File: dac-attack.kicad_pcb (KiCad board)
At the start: 2 copper layers, 31.1 x 43.8 mm, 59 parts, among them J1 BOARD, J2 BOARD, J3 BOARD, J4 ANALOG, J5 DIGITAL, J6 USER, J7 BTN, U1 CS8416-xZZ, U2 PCM5100, U3 SD6210A, U4 XC6206P332MR, U5 XC6206P332MR

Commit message: Initial work on revision 2023b.
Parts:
- removed the J2 at (95.2, 104.1)
- removed the J6 at (92.7, 90.8)
- removed the R9 at (100.3, 108.6)
- added C25: 22nF, Capacitor_SMD:C_0402_1005Metric, F.Cu at (155.6, 79.6)
- added H1: MountingHole, MountingHole:MountingHole_3.2mm_M3, F.Cu at (107.3, 72.4)
- added H2: MountingHole, MountingHole:MountingHole_3.2mm_M3, F.Cu at (169.0, 72.4)
- added J5: USER, Connector_PinHeader_2.54mm:PinHeader_1x02_P2.54mm_Vertical, B.Cu at (148.6, 88.3)
- added J7: BTN, Connector_JST:JST_SH_SM02B-SRSS-TB_1x02-1MP_P1.00mm_Horizontal, F.Cu at (128.3, 87.5)
- added R10: 10K, Resistor_SMD:R_0402_1005Metric, F.Cu at (163.2, 85.7)
- added R8: 47K, Resistor_SMD:R_0402_1005Metric, F.Cu at (156.8, 68.6)
- added TP1: GND, TestPoint:TestPoint_Keystone_5000-5004_Miniature, F.Cu at (104.8, 67.3)
- added TP2: GND, TestPoint:TestPoint_Keystone_5000-5004_Miniature, F.Cu at (171.4, 67.3)
- added TP3: 5V, TestPoint:TestPoint_Pad_D1.0mm, F.Cu at (162.6, 66.7)
- added TP4: 3V3, TestPoint:TestPoint_Pad_D1.0mm, F.Cu at (137.8, 74.9)
- added TP5: 3V3A, TestPoint:TestPoint_Pad_D1.0mm, F.Cu at (116.8, 71.8)
- added U6: TCM809, Package_TO_SOT_SMD:SOT-23, F.Cu at (159.4, 69.8)
- J1: footprint Connector_PinSocket_2.54mm:PinSocket_2x02_P2.54mm_Vertical -> Connector_PinHeader_2.54mm:PinHeader_1x04_P2.54mm_Vertical; moved to B.Cu
- moved C15 90.6 mm to (160.0, 72.4)
- moved FB1 89.2 mm to (160.7, 77.5), turned to -90 degrees
- moved C1 86.7 mm to (158.8, 77.5), turned to 90 degrees
- moved C23 83.2 mm to (156.8, 75.6), turned to -90 degrees
- moved C16 82.6 mm to (155.6, 77.6), turned to 90 degrees
- moved C28 81.6 mm to (155.6, 75.6), turned to -90 degrees
- moved R9 81.5 mm to (156.2, 73.7), turned to 180 degrees
- moved R3 75.6 mm to (153.0, 69.8), turned to 180 degrees
- moved C6 74.8 mm to (169.7, 78.7), turned to 90 degrees
- moved U1 74.4 mm to (149.9, 76.2), turned to 180 degrees
- moved C10 73.8 mm to (171.6, 79.4), turned to 90 degrees
- moved J1 73.7 mm to (171.4, 88.3), turned to 90 degrees
- moved J2 72.5 mm to (156.8, 87.5)
- moved G*** 72.0 mm to (153.0, 72.4)
- moved U3 70.4 mm to (166.5, 79.4), turned to 0 degrees
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- renumbered C25 to C26, C26 to C27, C27 to C28, J3 to J2, J4 to J3, J5 to J4, J7 to J6, R8 to R9
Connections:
- net /DDAT renamed /D_OUT
- C15 pad 1: GND -> +3V3
- C15 pad 2: Net-(C15-Pad2) -> GND
- C24 pad 1: /DOUT -> /D_IN
- J1 pad 1: /BUTTON -> GND
- J1 pad 2: /DOUT -> /VIN
- J1 pad 3: GND -> /D_IN
- J1 pad 4: /VIN -> /BUTTON
- J2 pad 4: /DOUT -> /D_IN
- J2 pad MP: unconnected-(J3-PadMP) -> GND
- U1 pad 5: Net-(C15-Pad2) -> Net-(C25-Pad2)
- U1 pad 9: +3V3 -> Net-(R8-Pad2)
- U3 pad 1: /VIN -> +5V
- U3 pad 5: +5V -> /VIN
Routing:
- net +5V: track 22.9 -> 60.3 mm
- net /D_IN: track 0.00 -> 19.3 mm
- net /DOUT: track 18.6 -> 0.00 mm, vias 2 -> 0
- net +3.3VA: track 52.1 -> 33.6 mm
- net /BUTTON: track 37.2 -> 50.8 mm, vias 3 -> 4
- net +3V3: track 87.0 -> 73.7 mm
- net Net-(R8-Pad2): track 0.00 -> 11.7 mm, vias 0 -> 2
- net /USER: track 15.5 -> 4.57 mm, vias 2 -> 1
- net Net-(J7-Pad2): track 2.54 -> 12.8 mm, vias 0 -> 2
- net /VIN: track 35.9 -> 42.4 mm
- net Net-(R15-Pad1): track 7.03 -> 13.0 mm
- net Net-(R1-Pad1): track 9.21 -> 14.7 mm
- net /RIGHT: track 15.5 -> 11.3 mm
- net /ADAT: track 10.3 -> 13.9 mm
- net Net-(C24-Pad2): track 11.7 -> 8.20 mm
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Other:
- board size 31.1 x 43.8 mm -> 71.8 x 26 mm
- board text added: "3V"
- board text added: "B_READ"
- board text added: "D_IN"
- board text added: "EXT BUTTON"
- board text added: "GND"
- board text added: "Rev 2023b Licensed under CERN-OHL-S v2"
- board text removed: "BTN"
- board text removed: "Rev 2023a Licensed under CERN-OHL-S v2"
- board text removed: "←MEMORY ←CARD"

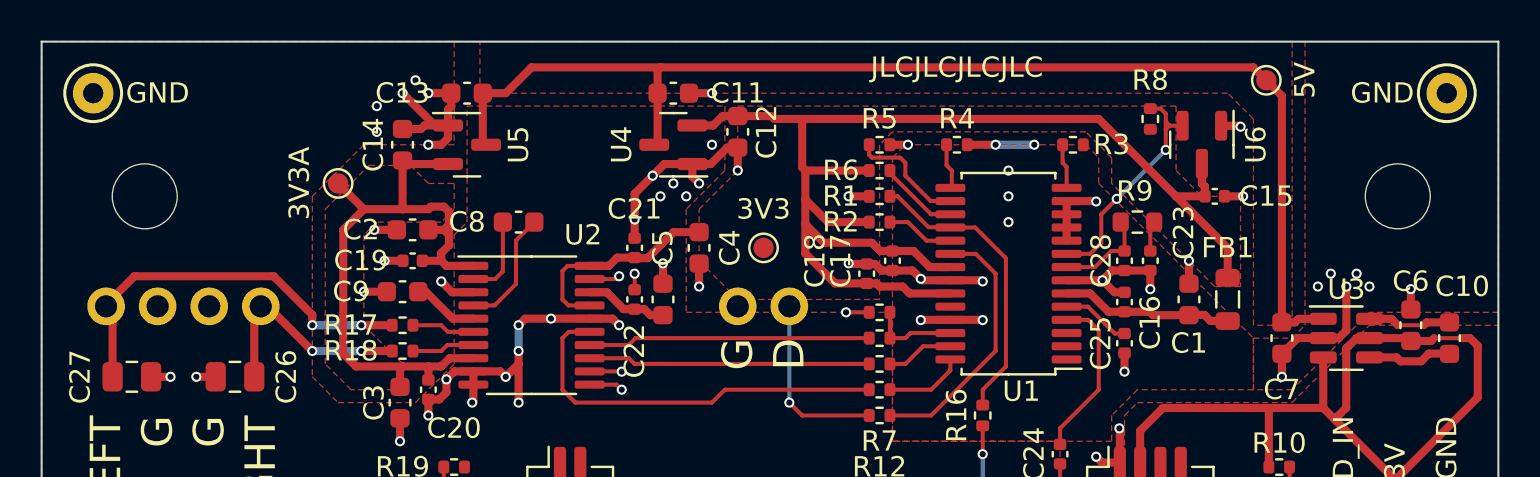
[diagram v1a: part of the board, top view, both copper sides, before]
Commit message: Tweaks to 2023b
Fixed one net, widened traces, made some minor silkscreen changes.
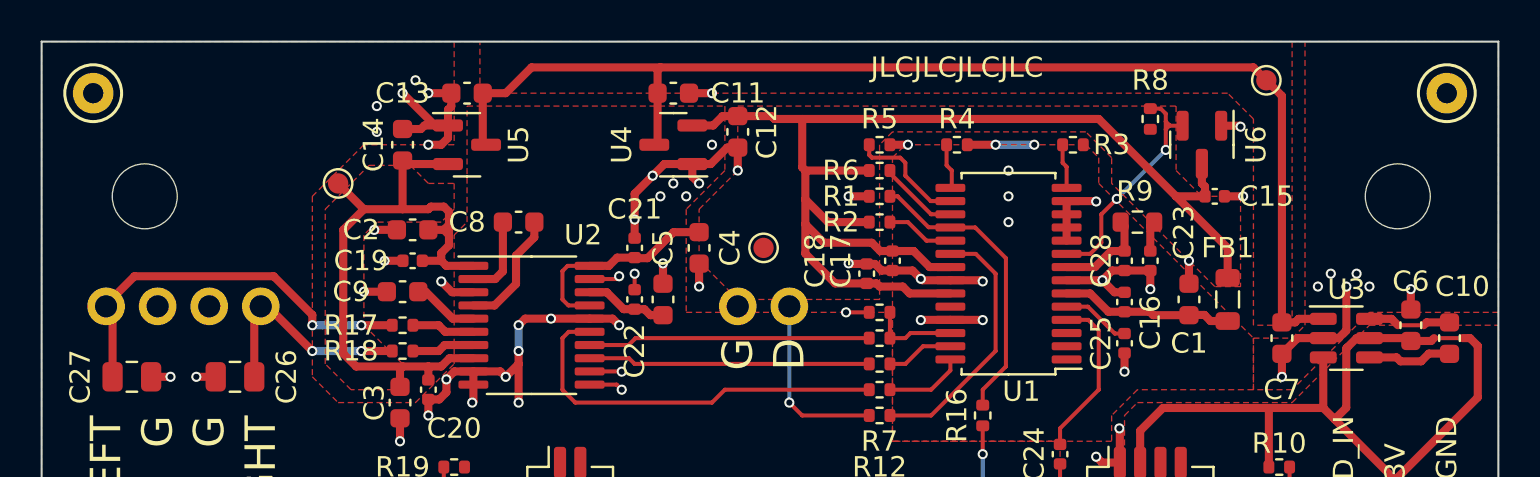
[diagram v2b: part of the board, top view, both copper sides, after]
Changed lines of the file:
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@@
   (net 39 "unconnected-(U1-Pad24)")
   (net 40 "Net-(R8-Pad2)")
-  (net 41 "Net-(J7-Pad2)")
+  (net 41 "Net-(J6-Pad2)")
   (net 42 "/D_IN")
   (net 43 "/D_OUT")
@@
       (net 18 "/BUTTON") (pinfunction "Pin_1") (pintype "passive"))
     (pad "2" smd roundrect (at 0.5 -2) (size 0.6 1.55) (layers "F.Cu" "F.Paste" "F.Mask") (roundrect_rratio 0.25)
-      (net 41 "Net-(J7-Pad2)") (pinfunction "Pin_2") (pintype "passive"))
+      (net 41 "Net-(J6-Pad2)") (pinfunction "Pin_2") (pintype "passive"))
     (pad "MP" smd roundrect (at 1.8 1.875) (size 1.2 1.8) (layers "F.Cu" "F.Paste" "F.Mask") (roundrect_rratio 0.2083333333)
       (net 2 "GND") (pinfunction "MountPin") (pintype "passive"))
@@
       (effects (font (size 1 1) (thickness 0.15)))
     )
-    (fp_text value "3V3" (at 0 1.905) (layer "F.SilkS")
+    (fp_text value "3V3" (at 0 1.905) (layer "F.SilkS") hide
       (effects (font (size 1 1) (thickness 0.15)))
     )
@@
       (effects (font (size 1 1) (thickness 0.15)))
     )
-    (fp_text value "GND" (at -3.175 0) (layer "F.SilkS")
+    (fp_text value "GND" (at -3.175 0) (layer "F.Fab")
       (effects (font (size 1 1) (thickness 0.15)))
     )
@@
       (effects (font (size 1 1) (thickness 0.15)))
     )
-    (fp_text value "GND" (at 3.175 0 180) (layer "F.SilkS")
+    (fp_text value "GND" (at 3.175 0 180) (layer "F.Fab")
       (effects (font (size 1 1) (thickness 0.15)))
     )
@@
     (property "Sheetname" "")
     (attr exclude_from_pos_files)
-    (fp_text reference "TP3" (at 0 -1.448) (layer "F.SilkS") hide
+    (fp_text reference "TP3" (at 0 -1.448) (layer "F.Fab") hide
       (effects (font (size 1 1) (thickness 0.15)))
     )
-    (fp_text value "5V" (at 1.905 0 90) (layer "F.SilkS")
+    (fp_text value "5V" (at 1.905 0 90) (layer "F.Fab")
       (effects (font (size 1 1) (thickness 0.15)))
     )
@@
       (net 2 "GND") (pintype "passive"))
     (pad "2" smd roundrect (at 0.51 0 180) (size 0.54 0.64) (layers "F.Cu" "F.Paste" "F.Mask") (roundrect_rratio 0.25)
-      (net 41 "Net-(J7-Pad2)") (pintype "passive"))
+      (net 41 "Net-(J6-Pad2)") (pintype "passive"))
     (model "${KICAD6_3DMODEL_DIR}/Resistor_SMD.3dshapes/R_0402_1005Metric.wrl"
       (offset (xyz 0 0 0))
@@
       (effects (font (size 1 1) (thickness 0.15)))
     )
-    (fp_text value "3V3A" (at -1.905 0 90) (layer "F.SilkS")
+    (fp_text value "3V3A" (at -1.905 0 90) (layer "F.Fab")
       (effects (font (size 1 1) (thickness 0.15)))
     )
@@
       (net 18 "/BUTTON") (pinfunction "Pin_1") (pintype "passive"))
     (pad "2" thru_hole oval (at 0 -2.54 90) (size 1.7 1.7) (drill 1) (layers *.Cu *.Mask)
-      (net 41 "Net-(J7-Pad2)") (pinfunction "Pin_2") (pintype "passive"))
+      (net 41 "Net-(J6-Pad2)") (pinfunction "Pin_2") (pintype "passive"))
     (model "${KICAD6_3DMODEL_DIR}/Connector_PinHeader_2.54mm.3dshapes/PinHeader_1x02_P2.54mm_Vertical.wrl"
       (offset (xyz 0 0 0))
@@
   (segment (start 123.965 67.31) (end 123.965 69.6875) (width 0.4) (layer "F.Cu") (net 7))
   (segment (start 132.715 66.04) (end 161.925 66.04) (width 0.4) (layer "F.Cu") (net 7))
-  (segment (start 124.955 73.66) (end 124.955 76.086) (width 0.2) (layer "F.Cu") (net 8))
-  (segment (start 124.576 76.465) (end 123.5025 76.465) (width 0.2) (layer "F.Cu") (net 8))
-  (segment (start 124.955 76.086) (end 124.576 76.465) (width 0.2) (layer "F.Cu") (net 8))
-  (segment (start 125.603 76.708) (end 125.603 74.562) (width 0.2) (layer "F.Cu") (net 9))
-  (segment (start 125.603 76.708) (end 124.546 77.765) (width 0.2) (layer "F.Cu") (net 9))
-  (segment (start 125.603 74.562) (end 126.505 73.66) (width 0.2) (layer "F.Cu") (net 9))
-  (segment (start 124.546 77.765) (end 123.5025 77.765) (width 0.2) (layer "F.Cu") (net 9))
+  (segment (start 124.576 76.465) (end 124.955 76.086) (width 0.4) (layer "F.Cu") (net 8))
+  (segment (start 124.955 76.086) (end 124.955 73.66) (width 0.4) (layer "F.Cu") (net 8))
+  (segment (start 123.5025 76.465) (end 124.576 76.465) (width 0.4) (layer "F.Cu") (net 8))
+  (segment (start 125.603 75.311) (end 125.603 76.708) (width 0.4) (layer "F.Cu") (net 9))
+  (segment (start 125.603 76.708) (end 124.546 77.765) (width 0.4) (layer "F.Cu") (net 9))
+  (segment (start 126.505 73.66) (end 126.505 74.409) (width 0.4) (layer "F.Cu") (net 9))
+  (segment (start 126.505 74.409) (end 125.603 75.311) (width 0.4) (layer "F.Cu") (net 9))
+  (segment (start 124.546 77.765) (end 123.5025 77.765) (width 0.4) (layer "F.Cu") (net 9))
   (segment (start 122.484 78.415) (end 121.158 77.089) (width 0.4) (layer "F.Cu") (net 10))
   (segment (start 123.5025 78.415) (end 122.484 78.415) (width 0.4) (layer "F.Cu") (net 10))
@@
   (segment (start 153.771 77.825) (end 155.095 79.149) (width 0.2) (layer "F.Cu") (net 13))
   (segment (start 152.7225 77.825) (end 153.771 77.825) (width 0.2) (layer "F.Cu") (net 13))
-  (segment (start 156.845 75.085) (end 156.845 73.85) (width 0.2) (layer "F.Cu") (net 14))
-  (segment (start 156.845 73.85) (end 157.035 73.66) (width 0.2) (layer "F.Cu") (net 14))
+  (segment (start 156.845 73.85) (end 157.035 73.66) (width 0.4) (layer "F.Cu") (net 14))
+  (segment (start 156.845 75.085) (end 156.845 73.85) (width 0.4) (layer "F.Cu") (net 14))
   (segment (start 154.305 81.915) (end 152.4 83.82) (width 0.2) (layer "F.Cu") (net 15))
   (segment (start 154.305 78.994) (end 154.305 81.915) (width 0.2) (layer "F.Cu") (net 15))
@@
   (segment (start 149.225 80.01) (end 146.05 83.185) (width 0.2) (layer "F.Cu") (net 29))
   (segment (start 146.9975 75.225) (end 148.25 75.225) (width 0.2) (layer "F.Cu") (net 29))
-  (segment (start 122.215 79.715) (end 121.92 80.01) (width 0.2) (layer "F.Cu") (net 30))
-  (segment (start 123.5025 79.715) (end 122.215 79.715) (width 0.2) (layer "F.Cu") (net 30))
-  (segment (start 121.92 80.01) (end 120.525 80.01) (width 0.2) (layer "F.Cu") (net 30))
+  (segment (start 122.088 79.715) (end 121.793 80.01) (width 0.4) (layer "F.Cu") (net 30))
+  (segment (start 121.793 80.01) (end 120.525 80.01) (width 0.4) (layer "F.Cu") (net 30))
+  (segment (start 123.5025 79.715) (end 122.088 79.715) (width 0.4) (layer "F.Cu") (net 30))
   (segment (start 131.49 79.375) (end 131.15 79.715) (width 0.2) (layer "F.Cu") (net 31))
   (segment (start 143 79.375) (end 131.49 79.375) (width 0.2) (layer "F.Cu") (net 31))
@@
   (segment (start 135.89 81.915) (end 135.255 82.55) (width 0.2) (layer "F.Cu") (net 32))
   (segment (start 143 81.915) (end 135.89 81.915) (width 0.2) (layer "F.Cu") (net 32))
-  (segment (start 123.5025 79.065) (end 122.245 79.065) (width 0.2) (layer "F.Cu") (net 33))
-  (segment (start 121.92 78.74) (end 120.525 78.74) (width 0.2) (layer "F.Cu") (net 33))
-  (segment (start 122.245 79.065) (end 121.92 78.74) (width 0.2) (layer "F.Cu") (net 33))
+  (segment (start 123.5025 79.065) (end 122.118 79.065) (width 0.4) (layer "F.Cu") (net 33))
+  (segment (start 122.118 79.065) (end 121.793 78.74) (width 0.4) (layer "F.Cu") (net 33))
+  (segment (start 121.793 78.74) (end 120.525 78.74) (width 0.4) (layer "F.Cu") (net 33))
   (segment (start 129.2275 80.365) (end 131.165 80.365) (width 0.2) (layer "F.Cu") (net 34))
   (segment (start 131.445 80.645) (end 131.165 80.365) (width 0.2) (layer "F.Cu") (net 34))
   (segment (start 143 80.645) (end 131.445 80.645) (width 0.2) (layer "F.Cu") (net 34))
-  (segment (start 155.575 73.85) (end 155.385 73.66) (width 0.2) (layer "F.Cu") (net 35))
-  (segment (start 154.912 75.085) (end 155.575 75.085) (width 0.2) (layer "F.Cu") (net 35))
-  (segment (start 152.7225 75.875) (end 154.122 75.875) (width 0.2) (layer "F.Cu") (net 35))
-  (segment (start 154.122 75.875) (end 154.912 75.085) (width 0.2) (layer "F.Cu") (net 35))
-  (segment (start 155.575 75.085) (end 155.575 73.85) (width 0.2) (layer "F.Cu") (net 35))
+  (segment (start 154.122 75.875) (end 154.912 75.085) (width 0.4) (layer "F.Cu") (net 35))
+  (segment (start 152.7225 75.875) (end 154.122 75.875) (width 0.4) (layer "F.Cu") (net 35))
+  (segment (start 155.575 75.085) (end 155.575 73.85) (width 0.4) (layer "F.Cu") (net 35))
+  (segment (start 154.912 75.085) (end 155.575 75.085) (width 0.4) (layer "F.Cu") (net 35))
+  (segment (start 155.575 73.85) (end 155.385 73.66) (width 0.4) (layer "F.Cu") (net 35))
   (segment (start 156.845 68.07) (end 157.355 68.07) (width 0.2) (layer "F.Cu") (net 40))
   (segment (start 153.883 75.225) (end 154.432 74.676) (width 0.2) (layer "F.Cu") (net 40))

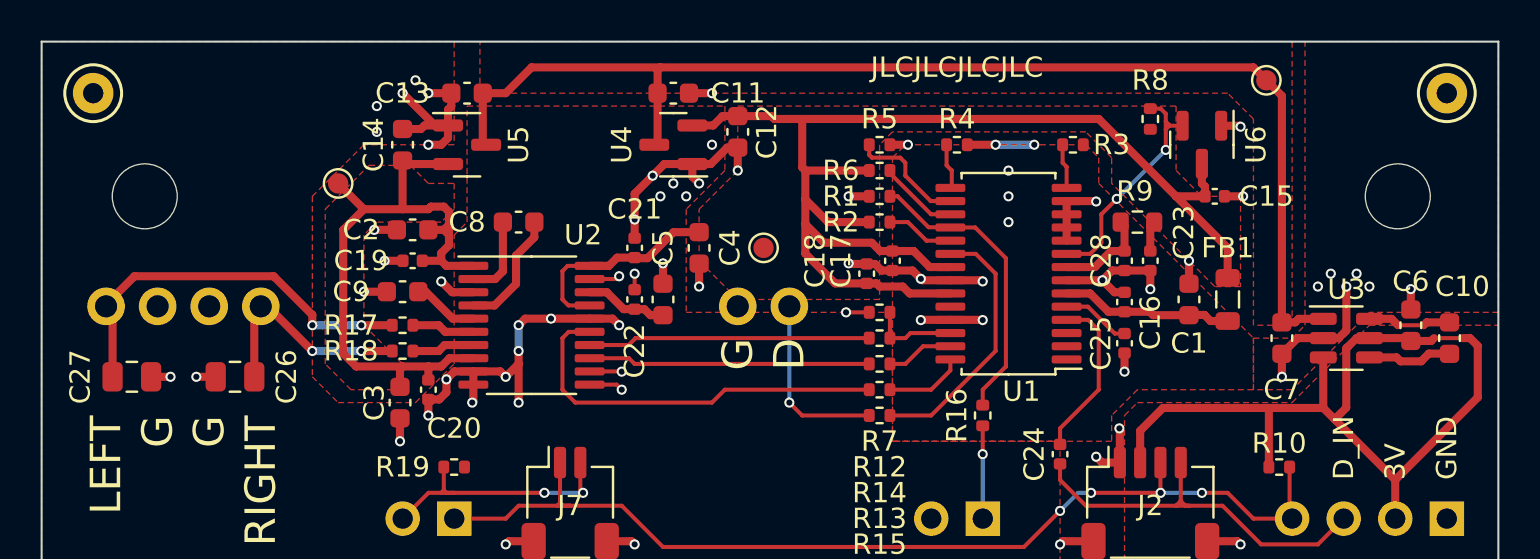
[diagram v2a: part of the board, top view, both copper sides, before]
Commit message: Board revision 2023c.
No component layout changes, just minor tweaks to mounting holes and silkscreening.
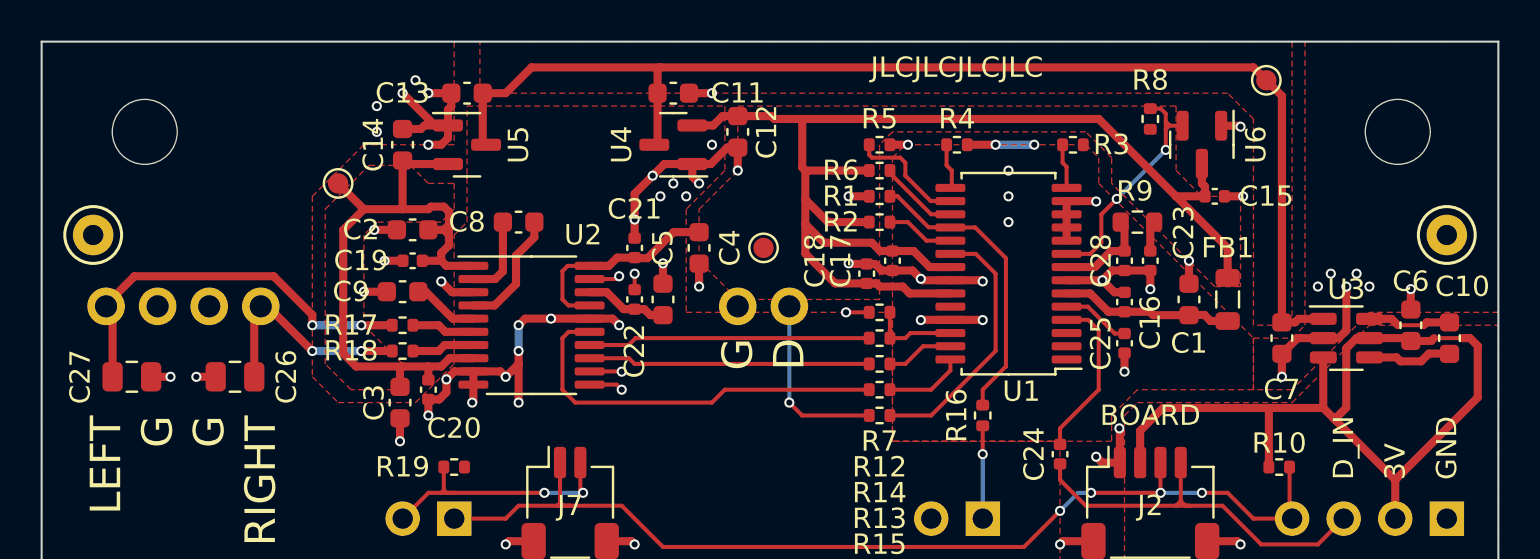
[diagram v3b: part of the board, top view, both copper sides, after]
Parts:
- moved TP1 6.98 mm to (104.8, 74.3)
- moved TP2 6.98 mm to (171.4, 74.3)
- moved G*** 5.75 mm to (152.4, 78.1)
- moved H1 3.17 mm to (107.3, 69.2)
- moved H2 3.17 mm to (169.0, 69.2)
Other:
- board text added: "BOARD"
- board text added: "DAC Attack! Rev 2023c Licensed under CERN-OHL-S v2 github.com/saybur/dac-attack"
- board text removed: "Rev 2023b Licensed under CERN-OHL-S v2"
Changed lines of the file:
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@@
   )
   (footprint "MountingHole:MountingHole_3.2mm_M3" (layer "F.Cu")
-    (at 169.035 72.39)
+    (at 169.035 69.215)
     (descr "Mounting Hole 3.2mm, no annular, M3")
     (tags "mounting hole 3.2mm no annular m3")
@@
   )
   (footprint "TestPoint:TestPoint_Keystone_5000-5004_Miniature" (layer "F.Cu")
-    (at 104.775 67.31 180)
+    (at 104.775 74.295 180)
     (descr "Keystone Miniature THM Test Point 5000-5004, http://www.keyelco.com/product-pdf.cfm?p=1309")
     (tags "Through Hole Mount Test Points")
@@
   )
   (footprint "TestPoint:TestPoint_Keystone_5000-5004_Miniature" (layer "F.Cu")
-    (at 171.45 67.31 180)
+    (at 171.45 74.295 180)
     (descr "Keystone Miniature THM Test Point 5000-5004, http://www.keyelco.com/product-pdf.cfm?p=1309")
     (tags "Through Hole Mount Test Points")
@@
   )
   (footprint "MountingHole:MountingHole_3.2mm_M3" (layer "F.Cu")
-    (at 107.315 72.39)
+    (at 107.315 69.215)
     (descr "Mounting Hole 3.2mm, no annular, M3")
     (tags "mounting hole 3.2mm no annular m3")
@@
   )
   (footprint "dac-attack:LOGO" (layer "B.Cu")
-    (at 153.035 72.39 180)
+    (at 152.4 78.105 180)
     (attr board_only exclude_from_pos_files exclude_from_bom)
     (fp_text reference "G***" (at 0 0) (layer "B.SilkS") hide
@@
     (effects (font (size 1 1) (thickness 0.15)) (justify mirror))
   )
-  (gr_text "Rev 2023b\nLicensed under\nCERN-OHL-S v2" (at 159.385 81.28) (layer "B.SilkS")
+  (gr_text "DAC Attack! Rev 2023c\nLicensed under CERN-OHL-S v2\ngithub.com/saybur/dac-attack" (at 163.83 68.58) (layer "B.SilkS")
     (effects (font (size 1 1) (thickness 0.15)) (justify left mirror))
   )
@@
     (effects (font (size 1.5 1.5) (thickness 0.3)) (justify right))
   )
+  (gr_text "BOARD" (at 156.845 83.185) (layer "F.SilkS")
+    (effects (font (size 1 1) (thickness 0.15)))
+  )
   (segment (start 152.7225 77.175) (end 153.883 77.175) (width 0.4) (layer "F.Cu") (net 1))
